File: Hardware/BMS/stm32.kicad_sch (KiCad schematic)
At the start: 13 parts, among them SW1 SW_SPDT, SW2 SW_MEC_5E, U1 STM32G473CCTx, Y1 48 MHZ

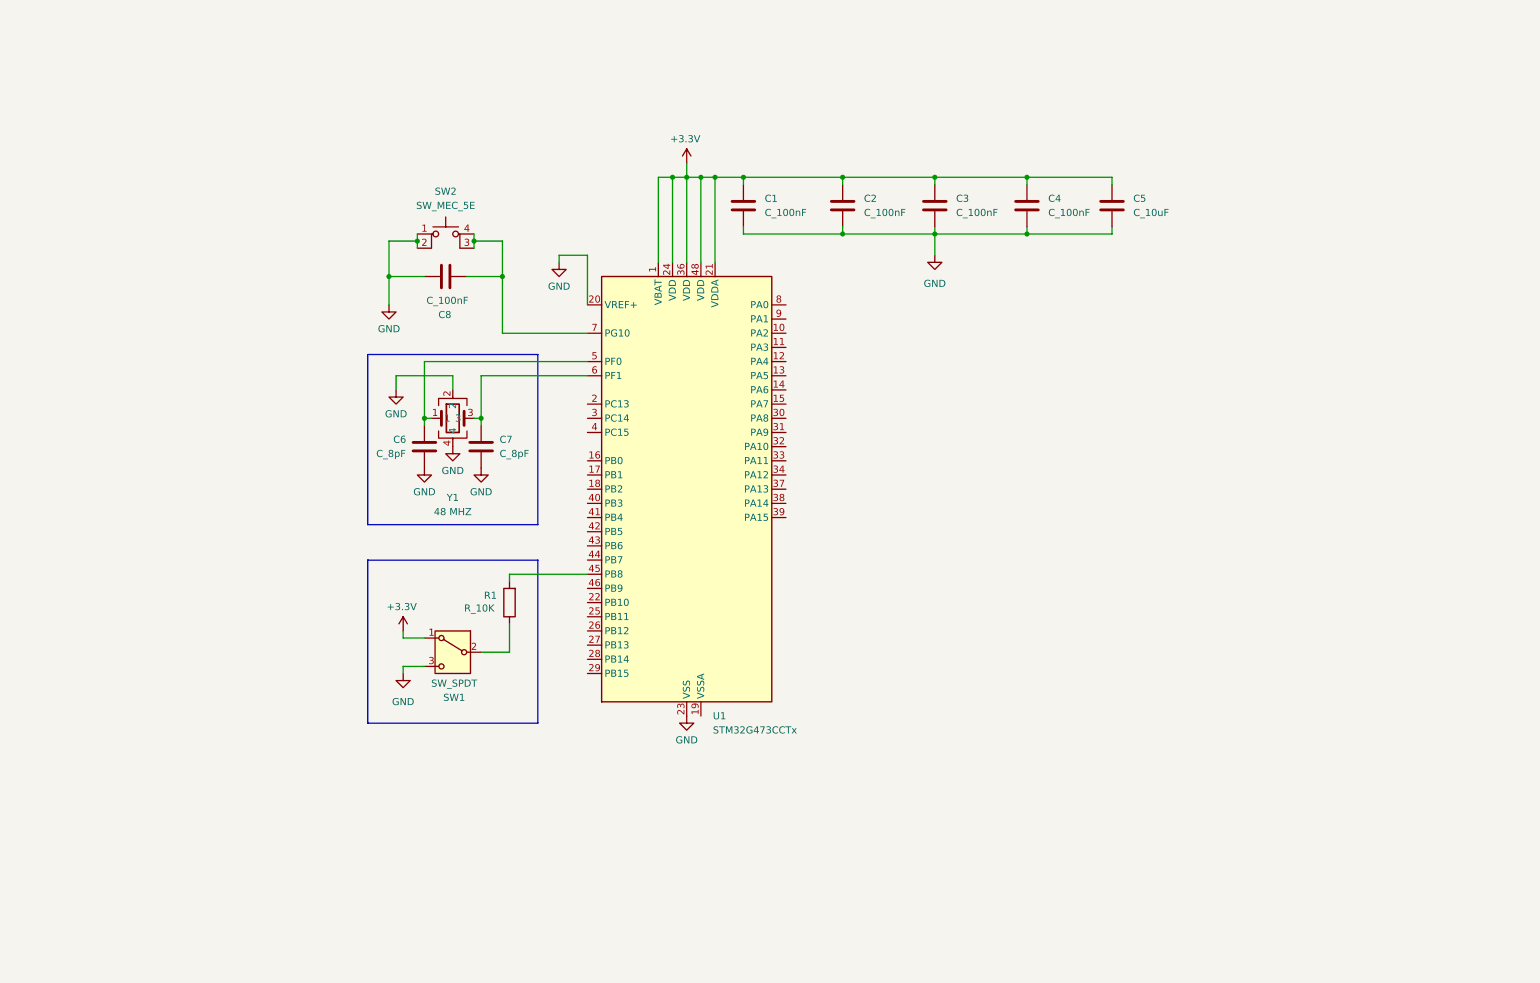
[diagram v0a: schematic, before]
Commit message: updated some stm stuff and added current sense amplifier for main pack
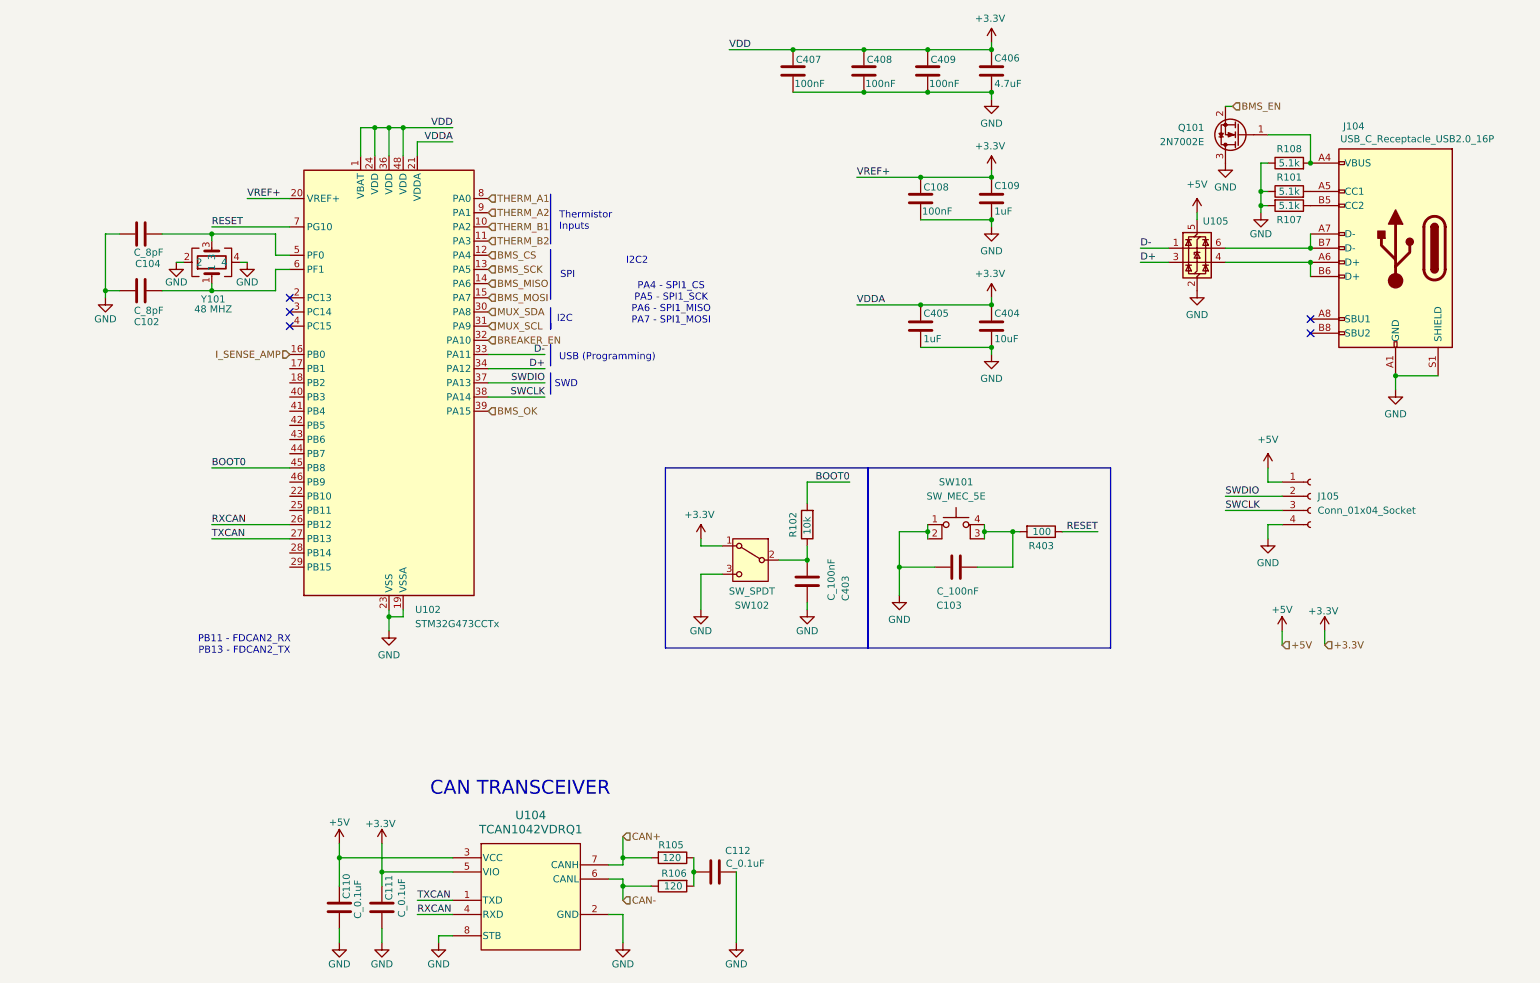
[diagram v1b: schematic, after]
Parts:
- removed C1, C2, C3: C_100nF, OEM:C_0603_1608Metric, symbol formula:C_100nF
- added C110, C111, C112: C_0.1uF, OEM:C_0603_1608Metric, symbol OEM:0u1F
- added C403: C_100nF, OEM:C_0603_1608Metric, symbol formula:C_100nF
- added C404: 10uF, Capacitor_SMD:C_0805_2012Metric, symbol formula:C_10uF
- added C405: 1uF, Capacitor_SMD:C_0603_1608Metric, symbol formula:C_10uF
- added C406: 4.7uF, Capacitor_SMD:C_0805_2012Metric, symbol formula:C_10uF
- added C407, C408, C409: 100nF, Capacitor_SMD:C_0603_1608Metric, symbol formula:C_100nF
- added J104: USB_C_Receptacle_USB2.0_16P, Connector_USB:USB_C_Receptacle_G-Switch_GT-USB-7051x, symbol Connector:USB_C_Receptacle_USB2.0_16P
- added J105: Conn_01x04_Socket, Connector_PinSocket_2.54mm:PinSocket_1x04_P2.54mm_Vertical, symbol Connector:Conn_01x04_Socket
- added Q101: 2N7002E, Package_TO_SOT_SMD:SOT-23, symbol Transistor_FET:2N7002E
- added R101, R107, R108: 5.1k, OEM:R_0603_1608Metric, symbol OEM:1KR
- added R105, R106: 120, OEM:R_0603_1608Metric, symbol OEM:120R_DNP
- added R403: 100, footprints:R_0805_OEM, symbol formula:R_10K
- added U104: TCAN1042VDRQ1, BAD_LIB:D0008A_M, symbol OlinBAD:TCAN1042VDRQ1
- added U105: USBLC6-2SC6, Package_TO_SOT_SMD:SOT-23-6, symbol Power_Protection:USBLC6-2SC6
- C108: renamed from C4; value C_100nF -> 100nF; footprint OEM:C_0603_1608Metric -> Capacitor_SMD:C_0603_1608Metric
- C109: renamed from C5; value C_10uF -> 1uF; footprint footprints:C_0805_OEM -> Capacitor_SMD:C_0603_1608Metric
- R102: renamed from R1; value R_10K -> 10k
- renumbered C6 to C102, C8 to C103, C7 to C104, SW2 to SW101, SW1 to SW102, U1 to U102, Y1 to Y101
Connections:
- net +3.3V: now also U102.20 (VREF+), C111.1, C404.1, C405.1, C406.1, C407.1, C408.1, C409.1, U104.5 (VIO)
- net GND: now also C102.1, U102.19 (VSSA), C110.2, C111.2, C112.2, C403.1, C404.2, C405.2, C406.2, C407.2, C408.2, C409.2, J104.A1 (GND), J104.A12 (GND), J104.B1 (GND), J104.B12 (GND), J104.S1 (SHIELD), J105.4 (Pin_4), Q101.3 (D), R101.1, R107.2, R108.1, U104.2 (GND), U104.8 (STB), U105.2 (GND); no longer C102.2, U102.20 (VREF+)
- net at C104.1, Y101.3: now also U102.5 (PF0); no longer U102.6 (PF1)
- net THERM_B1: now reaches U102.10 (PA2)
- net THERM_B2: now reaches U102.11 (PA3)
- net BMS_CS: now reaches U102.12 (PA4)
- net BMS_SCK: now reaches U102.13 (PA5)
- net BMS_MISO: now reaches U102.14 (PA6)
- net BMS_MOSI: now reaches U102.15 (PA7)
- net I_SENSE_AMP: now reaches U102.16 (PB0)
- net RXCAN: now reaches U102.26 (PB12)
- net RXCAN: now also U104.4 (RXD)
- net TXCAN: now reaches U102.27 (PB13)
- net TXCAN: now also U104.1 (TXD)
- net MUX_SDA: now reaches U102.30 (PA8)
- net MUX_SCL: now reaches U102.31 (PA9)
- net BREAKER_EN: now reaches U102.32 (PA10)
- net D-: now reaches U102.33 (PA11)
- net D-: now also U105.1 (I/O1)
- net D+: now reaches U102.34 (PA12)
- net D+: now also U105.3 (I/O2)
- net SWDIO: now reaches U102.37 (PA13)
- net SWDIO: now also J105.2 (Pin_2)
- net SWCLK: now reaches U102.38 (PA14)
- net SWCLK: now also J105.3 (Pin_3)
- net BMS_OK: now reaches U102.39 (PA15)
- net BOOT0: now reaches R102.2, U102.45 (PB8)
- net at C103.2, SW101.3 (K), SW101.4 (A): now also R403.2; no longer U102.7 (PG10)
- net THERM_A1: now reaches U102.8 (PA0)
- net THERM_A2: now reaches U102.9 (PA1)
- net at R102.1, SW102.2 (B): now also C403.2
- new net: C102.2, U102.6 (PF1), Y101.1
- new net: J104.A6 (D+), J104.B6 (D+), U105.4 (I/O2)
- new net: J104.A7 (D-), J104.B7 (D-), U105.6 (I/O1)
- new net: C112.1, R105.1, R106.2
- new net: J104.A4 (VBUS), J104.A9 (VBUS), J104.B4 (VBUS), J104.B9 (VBUS), Q101.1 (G), R108.2
- new net: J104.A5 (CC1), R101.2
- new net: J104.B5 (CC2), R107.1
- new net +5V: C110.1, J105.1 (Pin_1), U104.3 (VCC), U105.5 (VBUS)
- new net BMS_EN: Q101.2 (S)
- new net CAN+: R105.2, U104.7 (CANH)
- new net CAN-: R106.1, U104.6 (CANL)
- new net RESET: R403.1, U102.7 (PG10)
- no-connect marks 0 -> 5
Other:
- note added: "CAN TRANSCEIVER"
- note added: "I2C"
- note added: "I2C2"
- note added: "PA4 - SPI1_CS PA5 - SPI1_SCK PA6 - SPI1_MISO PA7 - SPI1_MOSI"
- note added: "PB11 - FDCAN2_RX PB13 - FDCAN2_TX"
- note added: "SPI"
- note added: "SWD"
- note added: "Thermistor Inputs"
- note added: "USB (Programming)"
- moved on the sheet: C102, C103, C104, C108, C109, R102, SW101, SW102, U102, Y101

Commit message: Add test points and LEDs
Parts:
- added D2: WHITE, LED_SMD:LED_0805_2012Metric, symbol Device:LED
- added R1: 400, Resistor_SMD:R_0603_1608Metric, symbol Device:R
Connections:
- net GND: now also R1.1
- net OV: now reaches U102.17 (PB1)
- net UV: now reaches U102.18 (PB2)
- net MUX2_COMS: now reaches U102.22 (PB10)
- net ADBMS_COMS: now reaches U102.25 (PB11)
- net DEBUG1: now reaches U102.28 (PB14)
- net BMS_HEARTBEAT: now reaches U102.29 (PB15)
- net OT: now reaches U102.40 (PB3)
- net UT: now reaches U102.41 (PB4)
- net ERROR: now reaches U102.42 (PB5)
- net USB_C_COMS: now reaches U102.43 (PB6)
- net CAN_COMS: now reaches U102.44 (PB7)
- net MUX1_COMS: now reaches U102.46 (PB9)
- net at J104.A4 (VBUS), J104.A9 (VBUS), J104.B4 (VBUS)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: now also D2.2 (A)
- new net: D2.1 (K), R1.2
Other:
- added sheet LEDs (leds.kicad_sch)
- moved on the sheet: C102, C104, U102, Y101

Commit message: begin layout
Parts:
- removed SW101: SW_MEC_5E, symbol Switch:SW_MEC_5E
- added SW402: SW_MEC_5G, Button_Switch_SMD:SW_MEC_5GSH9, symbol Switch:SW_MEC_5G
- SW401: renamed from SW102; footprint (none) -> Button_Switch_SMD:SW_SPDT_Shouhan_MSK12C02
- Y401: renamed from Y101; footprint footprints:SMD_72002_TXC -> footprints:Crystal_SMD_FA238
- renumbered C104 to C401, C102 to C402, C110 to C403, C111 to C404, C112 to C405, C407 to C406, C403 to C407, C108 to C409, C405 to C410, C409 to C411, C103 to C412, C406 to C413, C109 to C414, C404 to C415, D2 to D401, J105 to J401, J104 to J402, Q101 to Q401, R105 to R401, R106 to R402, R102 to R403, R403 to R404, R108 to R405, R101 to R406, R107 to R407, R1 to R408, U102 to U401, U104 to U402, U105 to U403
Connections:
- net GND: now also SW402.1 (A), SW402.2 (A)
- net at C412.2, R404.2: now also SW402.3 (B), SW402.4 (B)
